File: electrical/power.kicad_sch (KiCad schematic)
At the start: 44 parts

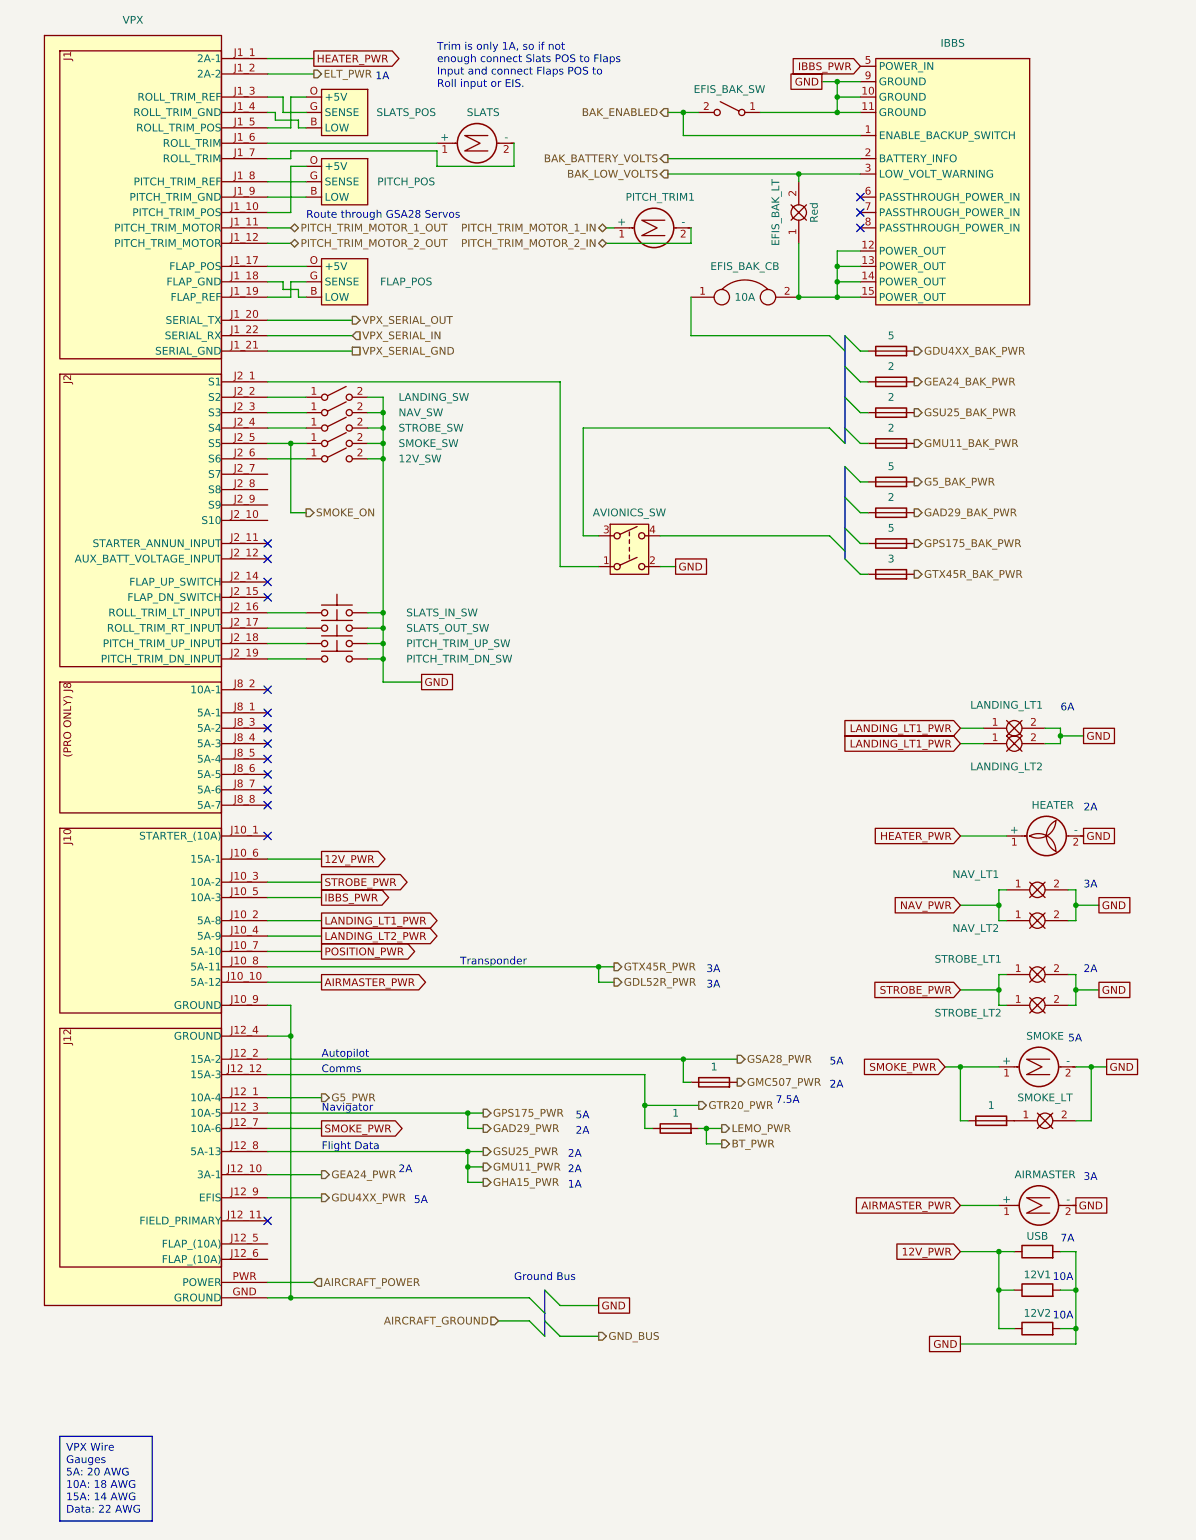
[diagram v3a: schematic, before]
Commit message: Converted to breakers w/GAD 27 instead of VP-X.
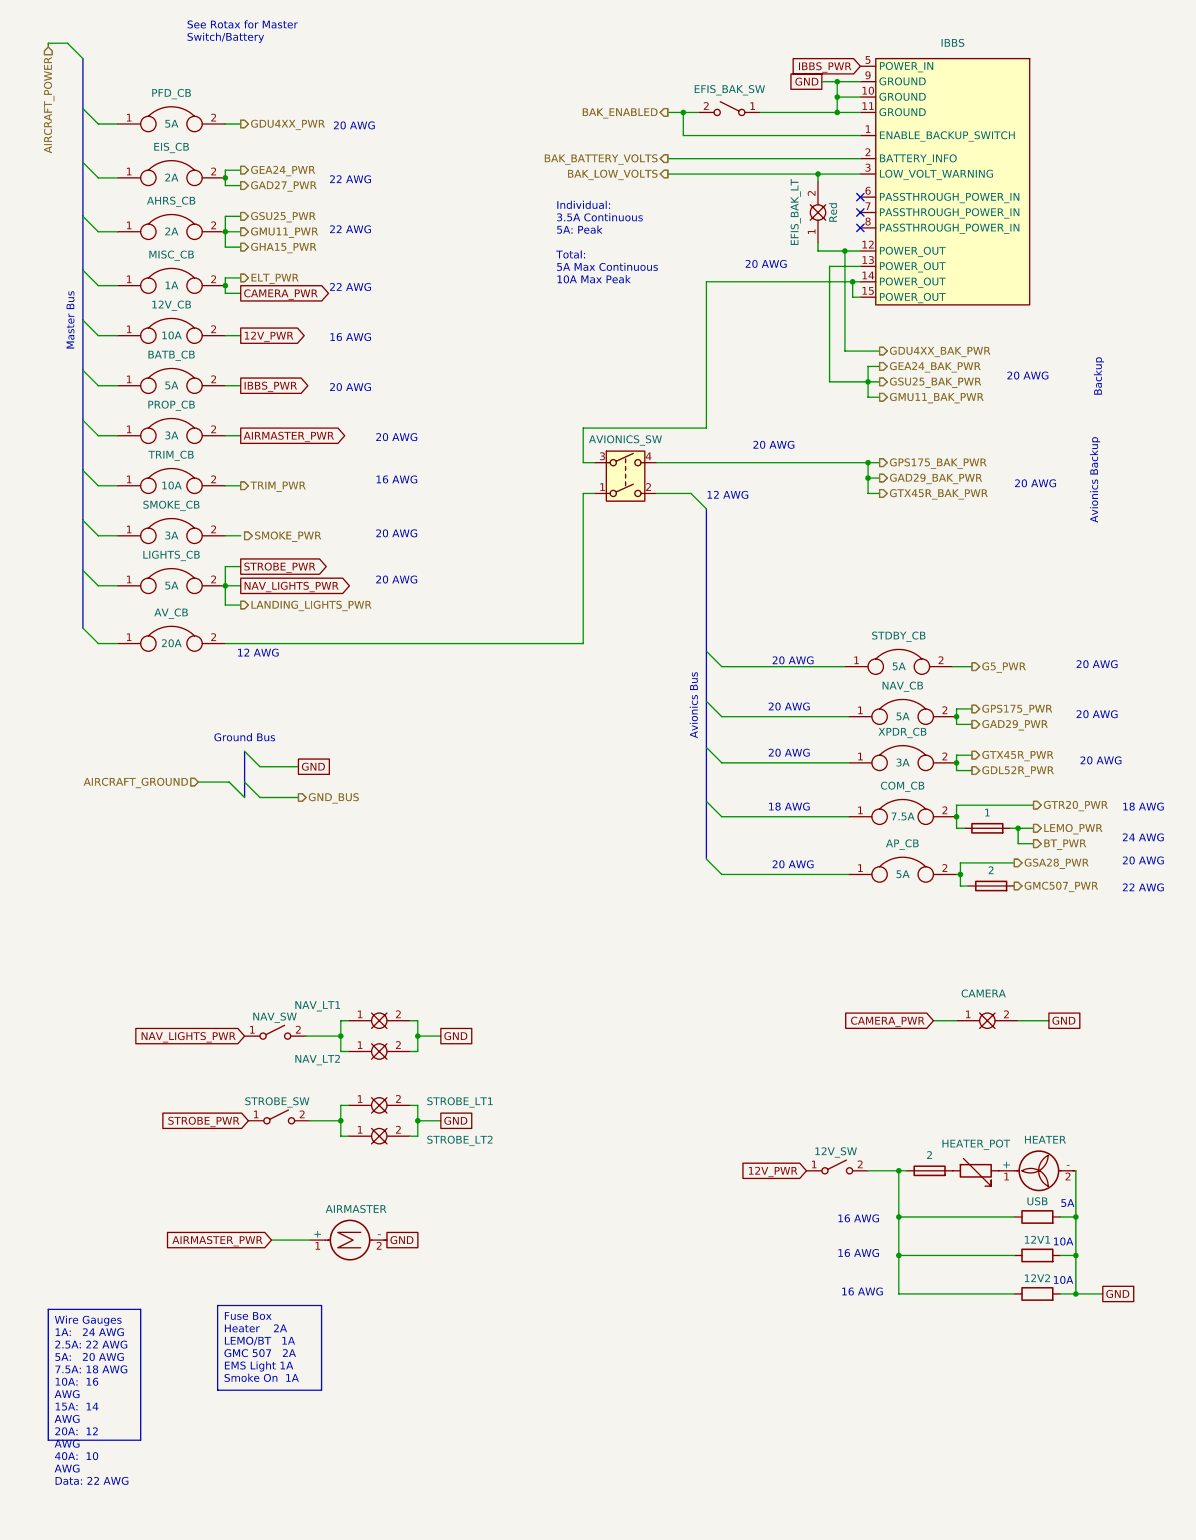
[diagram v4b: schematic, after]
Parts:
- removed BAK_G5_FS, BAK_GDU4XX_FS, BAK_GPS175_FS: 5, symbol Device:Fuse
- removed BAK_GAD29_FS, BAK_GEA24_FS, BAK_GMU11_FS, BAK_GSU25_FS: 2, symbol Device:Fuse
- removed BAK_GTX45R_FS: 3, symbol Device:Fuse
- removed EFIS_BAK_CB: 10A, symbol flyerx:Circuit_Breaker
- removed FLAP_POS, PITCH_POS, SLATS_POS: ~, symbol flyerx:Ray_Allen_POS-12
- removed LANDING_LT1, LANDING_LT2, SMOKE_LT: ~, symbol flyerx:Bulb
- removed LANDING_SW, SMOKE_SW: ~, symbol Switch:SW_SPST
- removed PITCH_TRIM1, SLATS, SMOKE: Motor_DC, symbol Motor:Motor_DC
- removed PITCH_TRIM_DN_SW, PITCH_TRIM_UP_SW, SLATS_IN_SW, SLATS_OUT_SW: SW_Push, symbol Switch:SW_Push
- removed SMOKE_LT_FS: 1, symbol Device:Fuse
- removed VPX: ~, symbol flyerx:Vertical_Power_VP-X
- added 12V_CB, TRIM_CB: 10A, symbol flyerx:Circuit_Breaker
- added AHRS_CB, EIS_CB: 2A, symbol flyerx:Circuit_Breaker
- added AP_CB, BATB_CB, LIGHTS_CB, NAV_CB, PFD_CB, STDBY_CB: 5A, symbol flyerx:Circuit_Breaker
- added AV_CB: 20A, symbol flyerx:Circuit_Breaker
- added CAMERA: Clear, symbol FlyerX:Bulb
- added COM_CB: 7.5A, symbol flyerx:Circuit_Breaker
- added HEATER_FS: 2, symbol Device:Fuse
- added HEATER_POT: R_Variable, symbol Device:R_Variable
- added MISC_CB: 1A, symbol flyerx:Circuit_Breaker
- added PROP_CB, SMOKE_CB, XPDR_CB: 3A, symbol flyerx:Circuit_Breaker
- GMC507_FS: value 1 -> 2
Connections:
- net 12V_PWR: now also 12V_SW.1 (A), 12V_CB.2; no longer 12V1.1, 12V2.1, USB.1
- net AIRMASTER_PWR: now also PROP_CB.2
- net G5_PWR: now also STDBY_CB.2
- net GAD29_BAK_PWR: now also AVIONICS_SW.4
- net GAD29_PWR: now also NAV_CB.2
- net GDL52R_PWR: now also XPDR_CB.2
- net GDU4XX_BAK_PWR: now also EFIS_BAK_LT.1, IBBS.12 (POWER_OUT)
- net GDU4XX_PWR: now also PFD_CB.2
- net GEA24_BAK_PWR: now also IBBS.13 (POWER_OUT)
- net GHA15_PWR: now also AHRS_CB.2
- net GND: now also CAMERA.2; no longer 12V_SW.2 (B), AVIONICS_SW.2, NAV_SW.2 (B), STROBE_SW.2 (B)
- net GSA28_PWR: now also AP_CB.2
- net GTR20_PWR: now also COM_CB.2
- net IBBS_PWR: now also BATB_CB.2
- net at AVIONICS_SW.1: now also AV_CB.2
- net NAV_LIGHTS_PWR: now reaches NAV_SW.1 (A)
- net NAV_LIGHTS_PWR: now also STROBE_SW.1 (A), LIGHTS_CB.2
- net at AVIONICS_SW.3: now also IBBS.14 (POWER_OUT), IBBS.15 (POWER_OUT)
- net HEATER_PWR: no longer names the net of HEATER.1 (+)
- net HEATER_PWR: now also HEATER_POT.1
- net NAV_PWR: no longer names the net of NAV_LT1.1, NAV_LT2.1
- net NAV_PWR: now also NAV_SW.2 (B)
- net STROBE_PWR: no longer names the net of STROBE_LT1.1, STROBE_LT2.1
- net STROBE_PWR: now also STROBE_SW.2 (B)
- new net: HEATER_FS.2, HEATER_POT.2
- new net: 12V1.1, 12V2.1, 12V_SW.2 (B), HEATER_FS.1, USB.1
- new net CAMERA_PWR: CAMERA.1, MISC_CB.2
- new net GAD27_PWR: EIS_CB.2
- new net TRIM_PWR: TRIM_CB.2
- no-connect marks 17 -> 3
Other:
- note added: "12 AWG"
- note added: "16 AWG"
- note added: "18 AWG"
- note added: "20 AWG"
- note added: "22 AWG"
- note added: "24 AWG"
- note added: "Avionics Backup"
- note added: "Avionics Bus"
- note added: "Backup"
- note added: "Individual: 3.5A Continuous 5A: Peak Total: 5A Max Continuous 10A Max Peak"
- note added: "Master Bus"
- note added: "See Rotax for Master Switch/Battery"
- note removed: "1A"
- note removed: "2A"
- note removed: "3A"
- note removed: "6A"
- note removed: "7.5A"
- note removed: "7A"
- note removed: "Autopilot"
- note removed: "Comms"
- note removed: "Flight Data"
- note removed: "Navigator"
- note removed: "Route through GSA28 Servos"
- note removed: "Transponder"
- note removed: "Trim is only 1A, so if not enough connect Slats POS to Flaps Input and connect Flaps POS to Roll input or EIS."
- moved on the sheet: 12V1, 12V2, 12V_SW, AIRMASTER, AVIONICS_SW, EFIS_BAK_LT, HEATER, NAV_LT1, NAV_LT2, NAV_SW, STROBE_LT1, STROBE_LT2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

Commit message: Unknown set of changes. Didn't spent time to look
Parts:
- MISC_CB: value 1A -> 2A
- SMOKE_CB: value 3A -> 5A
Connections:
- net SMOKE_PWR: now also SMOKE_CB.2
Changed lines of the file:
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@@
     (title "Power Distribution")
     (date "2024-03-15")
-    (rev "1.0")
+    (rev "1.0.1")
     (company "N915SN Angry Bird")
     (comment 1 "w/Breakers")
@@
   )
   (junction (at 46.355 57.785) (diameter 0) (color 0 0 0 0)
+  )
+  (junction (at 152.4 92.075) (diameter 0) (color 0 0 0 0)
   )
   (junction (at 144.145 39.37) (diameter 0) (color 0 0 0 0)
@@
     (stroke (width 0) (type default))
   )
+  (wire (pts (xy 154.305 94.615) (xy 152.4 94.615))
+    (stroke (width 0) (type default))
+  )
   (wire (pts (xy 46.355 110.49) (xy 46.355 107.315))
     (stroke (width 0) (type default))
@@
     (stroke (width 0) (type default))
   )
-  (wire (pts (xy 46.355 99.06) (xy 48.895 99.06))
+  (wire (pts (xy 46.355 99.06) (xy 49.53 99.06))
     (stroke (width 0) (type default))
   )
@@
   )
   (wire (pts (xy 167.005 143.51) (xy 179.705 143.51))
+    (stroke (width 0) (type default))
+  )
+  (wire (pts (xy 152.4 94.615) (xy 152.4 92.075))
     (stroke (width 0) (type default))
   )
@@
     (effects (font (size 1.27 1.27)) (justify left))
   )
+  (hierarchical_label "GMC507_BAK_PWR" (shape output) (at 154.305 94.615 0) (fields_autoplaced)
+    (effects (font (size 1.27 1.27)) (justify left))
+  )
   (hierarchical_label "GAD27_PWR" (shape output) (at 48.895 41.275 0) (fields_autoplaced)
     (effects (font (size 1.27 1.27)) (justify left))
@@
       (effects (font (size 1.27 1.27)))
     )
-    (property "Value" "1A" (at 37.465 57.785 0)
+    (property "Value" "2A" (at 37.465 57.785 0)
       (effects (font (size 1.27 1.27)))
     )
@@
       (effects (font (size 1.27 1.27)))
     )
-    (property "Value" "3A" (at 37.465 99.06 0)
-      (effects (font (size 1.27 1.27)))
-    )
+    (property "Value" "5A" (at 37.465 99.06 0)
+      (effects (font (size 1.27 1.27)))
+    )

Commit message: Interim check-in. Not sure what I was doing.
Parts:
- added LANDING_LT1, LANDING_LT2, LANDING_LT3, SMOKE_LT, WAG_LT3: ~, symbol flyerx:Bulb
- added LANDING_SW, SMOKE_SW, WAG_SW: ~, symbol Switch:SW_SPST
- added PITCH_TRIM, SLATS, SMOKE: Motor_DC, symbol Motor:Motor_DC
- added PITCH_TRIM_DN_SW, PITCH_TRIM_UP_SW, SLATS_IN_SW, SLATS_OUT_SW: SW_Push, symbol Switch:SW_Push
- added PITCH_TRIM_RELAY, SLATS_RELAY: EC2-12TNU, Relay_THT:Relay_DPDT_Kemet_EC2_DoubleCoil, symbol Relay:EC2-12TNU
- added SMOKE_LT_FS1: 1, symbol Device:Fuse
- added SMOKE_RELAY: ADW11, Relay_THT:Relay_1P1T_NO_10x24x18.8mm_Panasonic_ADW11xxxxW_THT, symbol Relay:ADW11
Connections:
- net GND: now also LANDING_LT1.2, LANDING_LT2.2, LANDING_LT3.2, PITCH_TRIM_RELAY.10, PITCH_TRIM_RELAY.12, PITCH_TRIM_RELAY.5, PITCH_TRIM_RELAY.7, SLATS_RELAY.10, SLATS_RELAY.12, SLATS_RELAY.5, SLATS_RELAY.7, SMOKE.2 (-), SMOKE_LT.2, SMOKE_SW.2 (B), WAG_LT3.2
- net SMOKE_PWR: now also SMOKE_RELAY.5, SMOKE_RELAY.6
- net GAD27_PWR renamed GEA24_PWR
- net NAV_LIGHTS_PWR renamed LANDING_LIGHTS_PWR
- net LANDING_LIGHTS_PWR: now also LANDING_SW.1 (A), WAG_SW.1 (A)
- net TRIM_PWR renamed SLATS_PWR
- net SLATS_PWR: now also PITCH_TRIM_DN_SW.1, PITCH_TRIM_RELAY.3, PITCH_TRIM_RELAY.8, PITCH_TRIM_UP_SW.1, SLATS_IN_SW.1, SLATS_OUT_SW.1, SLATS_RELAY.3, SLATS_RELAY.8
- new net: PITCH_TRIM_RELAY.1, PITCH_TRIM_UP_SW.2
- new net: PITCH_TRIM.1 (+), PITCH_TRIM_RELAY.4
- new net: PITCH_TRIM_DN_SW.2, PITCH_TRIM_RELAY.6
- new net: PITCH_TRIM.2 (-), PITCH_TRIM_RELAY.9
- new net: WAG_LT3.1, WAG_SW.2 (B)
- new net: LANDING_LT1.1, LANDING_LT2.1, LANDING_LT3.1, LANDING_SW.2 (B)
- new net: SLATS_IN_SW.2, SLATS_RELAY.1
- new net: SLATS.1 (+), SLATS_RELAY.4
- new net: SLATS.2 (-), SLATS_RELAY.9
- new net: SMOKE.1 (+), SMOKE_LT_FS1.1, SMOKE_RELAY.3
- new net: SMOKE_RELAY.1, SMOKE_SW.1 (A)
- new net: SLATS_OUT_SW.2, SLATS_RELAY.6
- new net SMOKE_ON: SMOKE_LT.1, SMOKE_LT_FS1.2
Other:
- note added: "Assumes Landing LT3 is AeroLED"
- note added: "Something already exists for these relays"
- moved on the sheet: 12V1, 12V2, 12V_SW, AIRMASTER, AP_CB, CAMERA, COM_CB, HEATER, HEATER_POT, NAV_CB, NAV_LT1, NAV_LT2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
